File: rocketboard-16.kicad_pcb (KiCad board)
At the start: 2 copper layers, 86.2 x 105.8 mm, 110 parts, among them J1 SWD, K1 MX_RGB, K10 MX_RGB, K11 MX_RGB, K12 MX_RGB, K13 MX_RGB, K14 MX_RGB, K15 MX_RGB, K16 MX_RGB, K2 MX_RGB, K3 MX_RGB, K4 MX_RGB, K5 MX_RGB, K6 MX_RGB, K7 MX_RGB, K8 MX_RGB, K9 MX_RGB, P1 USB_C_Plug_USB2.0, SW1 SW_Push, SW2 Rotary 1, SW3 Rotary 2, U1 STM32F103C8T6, U2 AMS1117-3.3, U3 USBLC6-2SC6, U4 SSD1306_128x64, X1 8 MHz, Y1 32.768 kHz

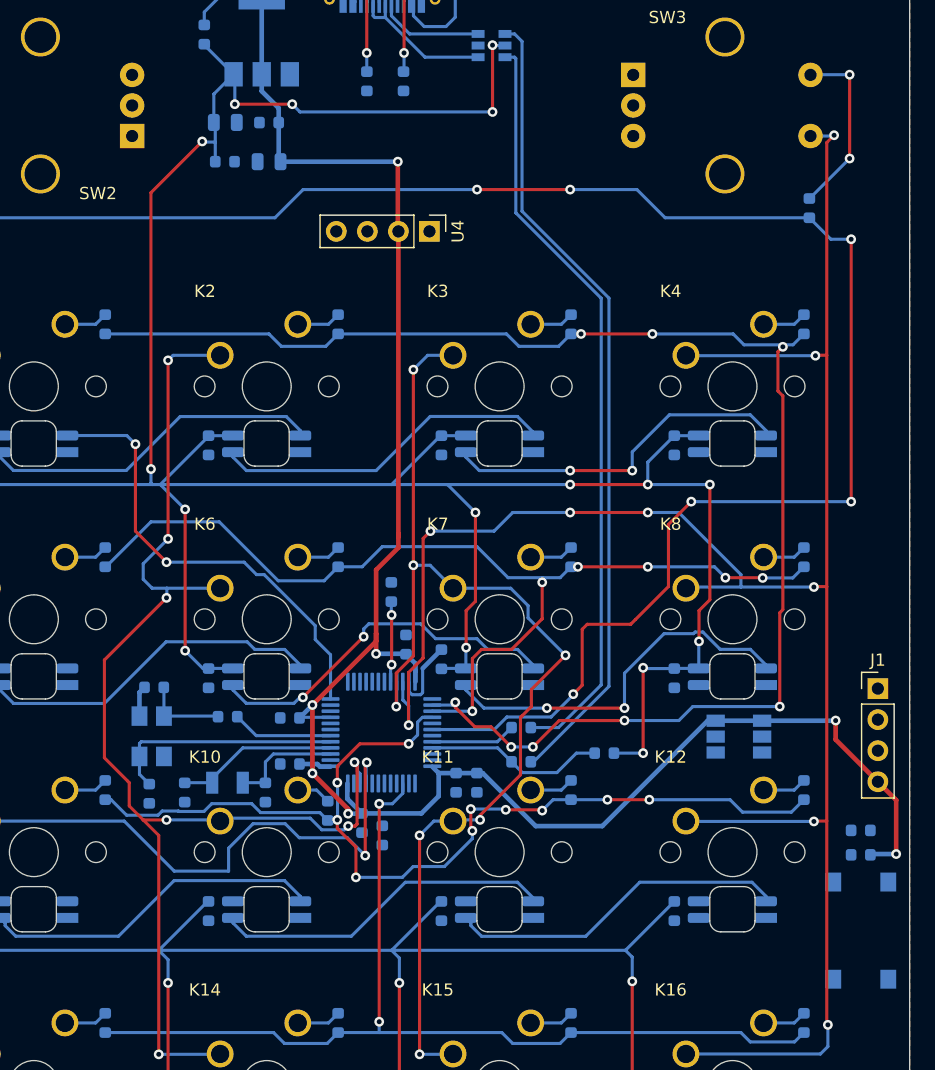
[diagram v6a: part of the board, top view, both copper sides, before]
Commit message: Routed more traces. Only lacking a few more connections except for ground. Had to move some pins around to make room, though the change did not help with routing so far.
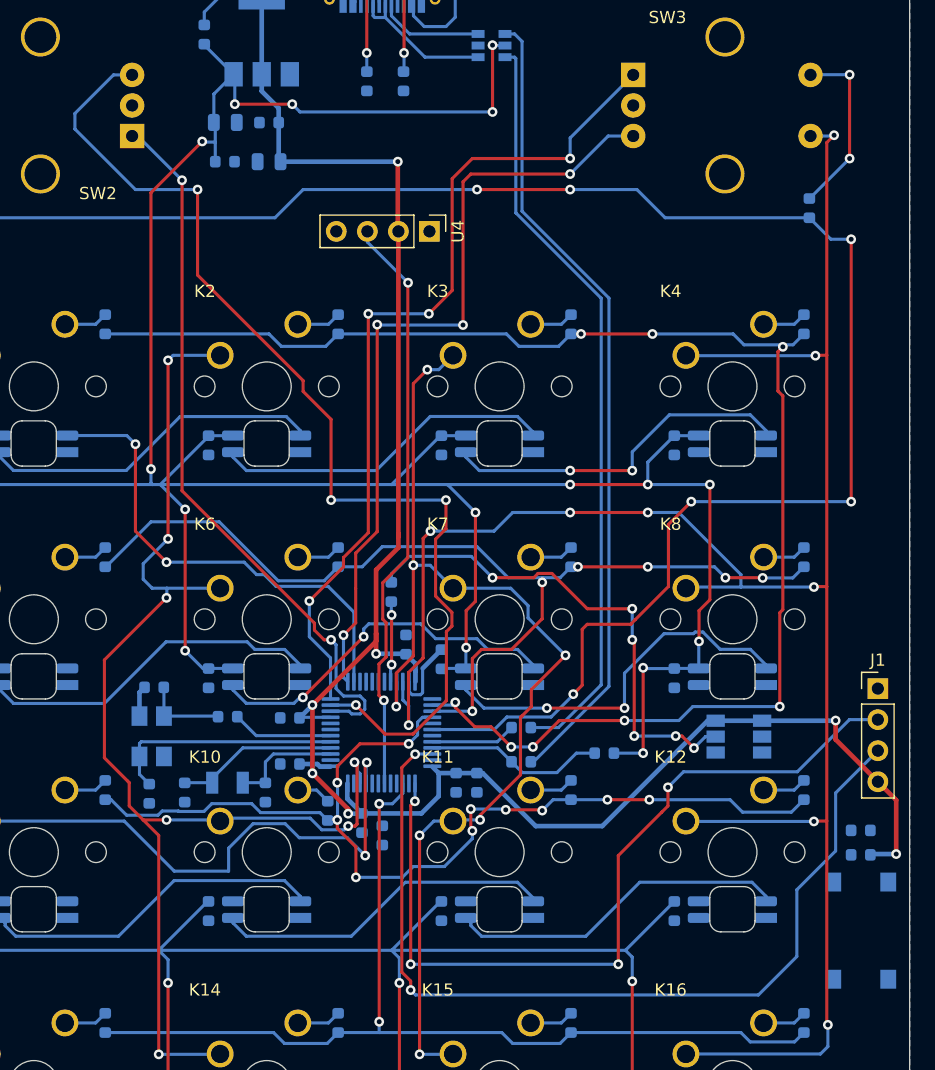
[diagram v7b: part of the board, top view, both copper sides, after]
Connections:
- U1 pad 12: LED_SIG -> EC2_A
- U1 pad 13: Net-(U1-Pad13) -> EC2_B
- U1 pad 14: Net-(U1-Pad14) -> LED_SIG
- U1 pad 16: EC2_A -> Net-(U1-Pad16)
- U1 pad 17: EC2_B -> Net-(U1-Pad17)
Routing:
- net EC1_B: track 0.00 -> 87.8 mm, vias 0 -> 4
- net SWDIO: track 0.00 -> 74.1 mm, vias 0 -> 2
- net EC2_A: track 0.00 -> 70.3 mm, vias 0 -> 4
- net SWCLK: track 0.00 -> 67.5 mm, vias 0 -> 4
- net EC2_B: track 0.00 -> 64.7 mm, vias 0 -> 4
- net EC1_A: track 0.00 -> 59.2 mm, vias 0 -> 2
- net SCL: track 0.00 -> 47.9 mm, vias 0 -> 2
- net BOOT1: track 0.00 -> 41.0 mm, vias 0 -> 6
- net LED_SIG: track 37.4 -> 39.3 mm
- net COL2: track 92.5 -> 91.8 mm

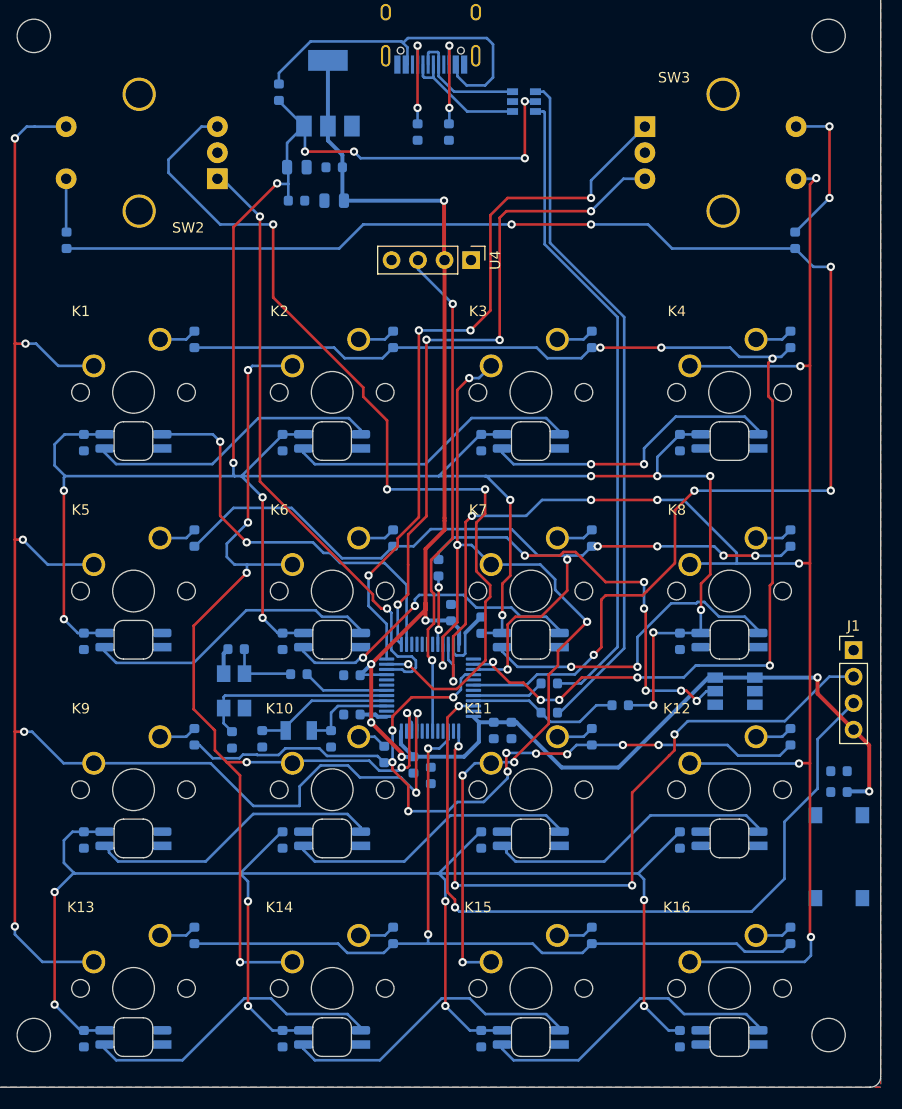
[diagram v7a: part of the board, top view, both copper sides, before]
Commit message: Finished all routing, very messy, but theoretically should work
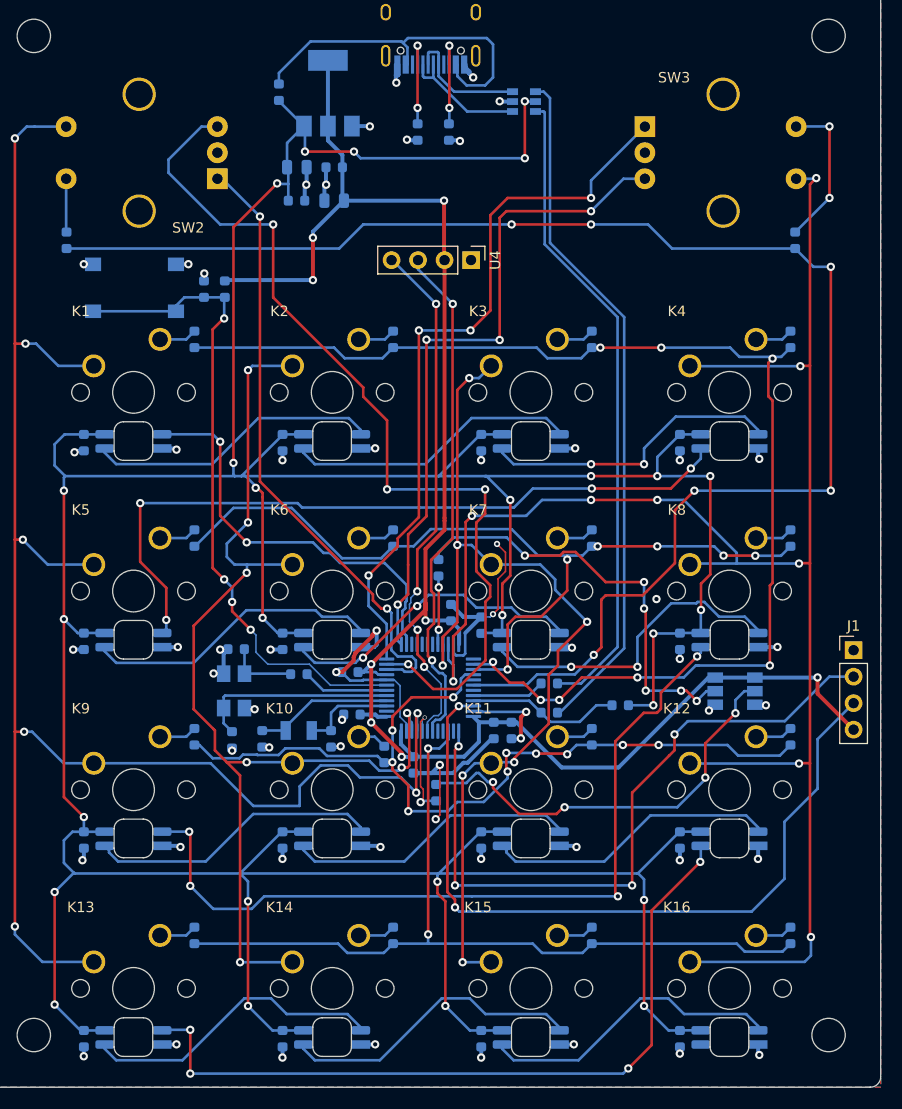
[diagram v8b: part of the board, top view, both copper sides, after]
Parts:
- moved SW1 86.8 mm to (94.7, 74.7), turned to 180 degrees
- moved C31 76.4 mm to (101.3, 74.8), turned to 270 degrees
- moved R3 76.1 mm to (103.3, 74.8), turned to 90 degrees
- moved R8 1.73 mm to (123.6, 123.1), turned to 90 degrees
- moved C7 0.36 mm to (115.3, 111.5)
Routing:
- net GND: track 8.78 -> 131.2 mm, vias 0 -> 59
- net LED_R2: track 0.00 -> 78.4 mm, vias 0 -> 4
- net LED_R3: track 0.00 -> 73.3 mm, vias 0 -> 4
- net LED_R1: track 0.00 -> 70.5 mm, vias 0 -> 4
- net Net-(C31-Pad2): track 0.00 -> 63.6 mm, vias 0 -> 4
- net SDA: track 0.00 -> 50.2 mm, vias 0 -> 4
- net BOOT0: track 0.00 -> 40.6 mm, vias 0 -> 4
- net +5V: track 404.7 -> 433.7 mm, vias 26 -> 27
- net Net-(R8-Pad1): track 0.00 -> 11.4 mm, vias 0 -> 2
- net VCC: track 161.9 -> 171.0 mm, vias 7 -> 8
- net SCL: track 47.9 -> 49.5 mm
- net Net-(D17-Pad2): track 34.0 -> 34.6 mm
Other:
- rule trace_min: 0.2 -> 0.1524
